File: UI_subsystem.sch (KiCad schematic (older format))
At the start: 1 part

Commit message: Created footprint and assigned it
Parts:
- TFT1: footprint (none) -> pwr_Beaglebone:ST7735
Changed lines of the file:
@@
 F 0 "TFT1" H 4550 1850 50  0000 R CNN
 F 1 "ST7735_TFT" H 4700 1950 50  0000 R CNN
-F 2 "" V 4527 1935 50  0001 C CNN
+F 2 "pwr_Beaglebone:ST7735" V 4527 1935 50  0001 C CNN
 F 3 "" V 4527 1935 50  0001 C CNN
 	1    3800 2750

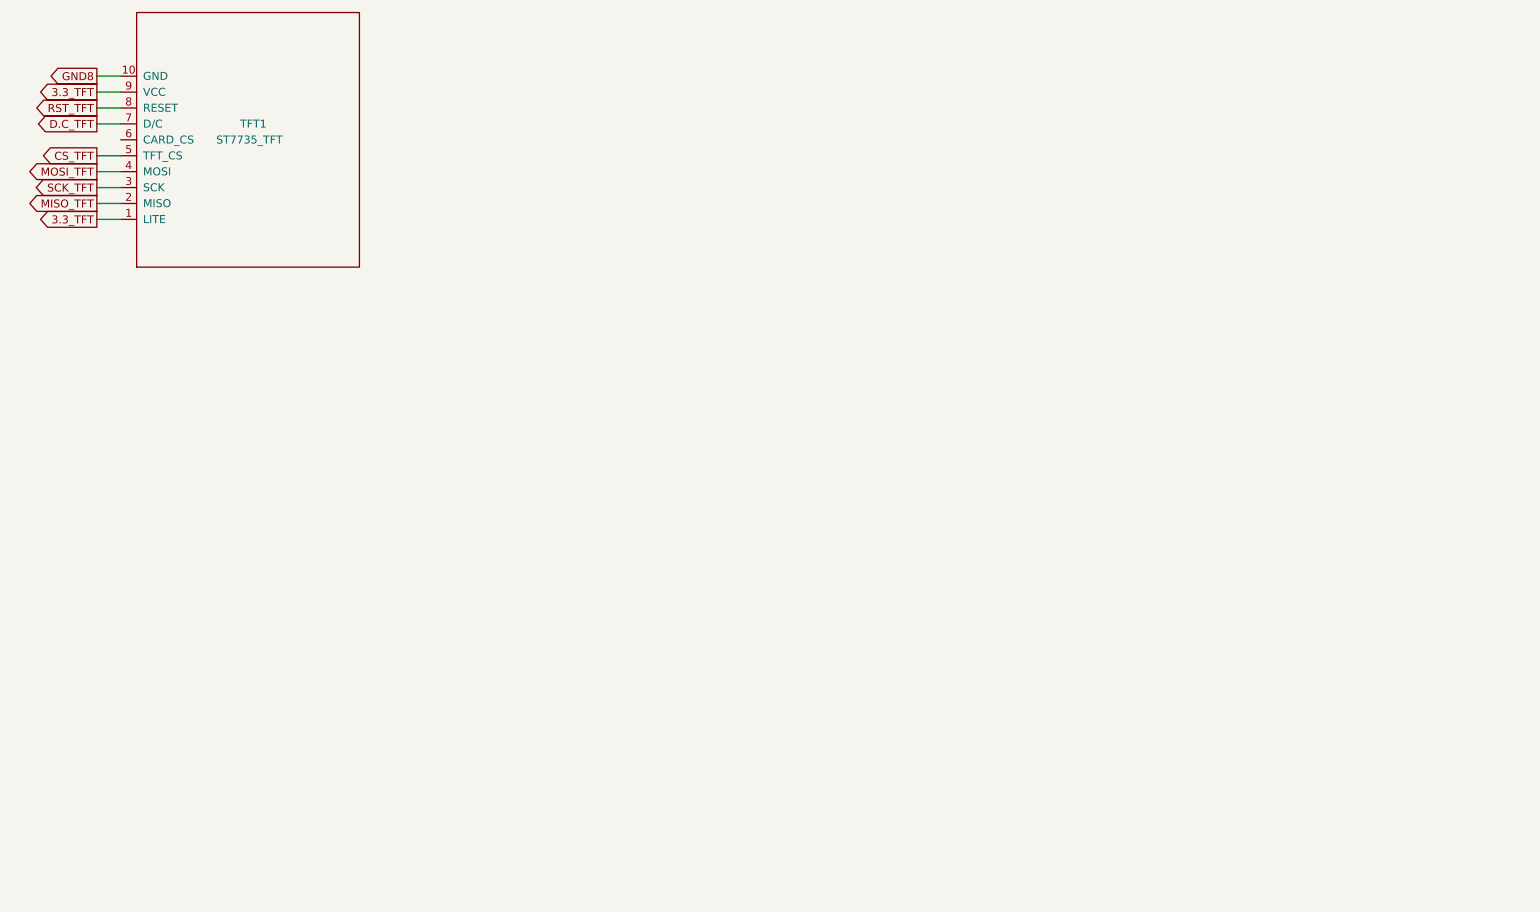
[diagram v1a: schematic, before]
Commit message: Added Buttons, LEDs and MCU to BB connections.
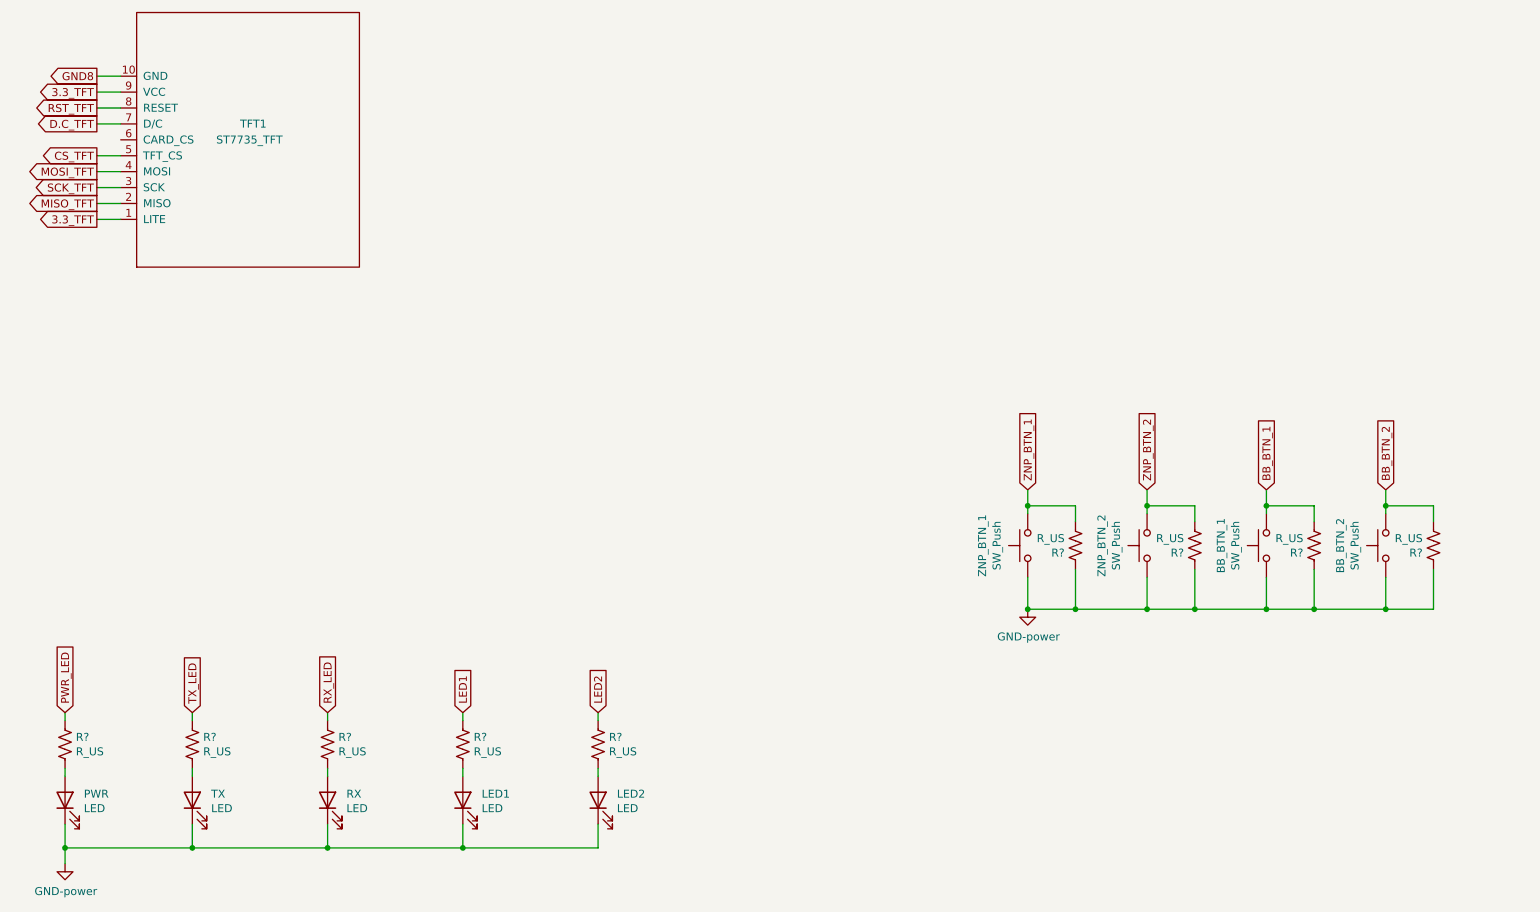
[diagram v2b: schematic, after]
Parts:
- added BB_BTN_1, BB_BTN_2, ZNP_BTN_1, ZNP_BTN_2: SW_Push, symbol Switch:SW_Push
- added LED1, LED2, PWR, RX, TX: LED, symbol Device:LED
- added R? (x9): R_US, symbol Device:R_US
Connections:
- new net: PWR.2 (A), R?.2
- new net: R?.2, TX.2 (A)
- new net: R?.2, RX.2 (A)
- new net: LED1.2 (A), R?.2
- new net: LED2.2 (A), R?.2
- new net BB_BTN_1: BB_BTN_1.2, R?.2
- new net BB_BTN_2: BB_BTN_2.2, R?.2
- new net GND: BB_BTN_1.1, BB_BTN_2.1, LED1.1 (K), LED2.1 (K), PWR.1 (K), R?.1, R?.1, R?.1, R?.1, RX.1 (K), TX.1 (K), ZNP_BTN_1.1, ZNP_BTN_2.1
- new net LED1: R?.1
- new net LED2: R?.1
- new net PWR_LED: R?.1
- new net RX_LED: R?.1
- new net TX_LED: R?.1
- new net ZNP_BTN_1: R?.2, ZNP_BTN_1.2
- new net ZNP_BTN_2: R?.2, ZNP_BTN_2.2

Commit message: Added Some Values
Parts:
- R? (x2): value R_US -> 100
- R? (x2): value R_US -> 10k
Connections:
- net labels added: +3V3
- wire segments 60 -> 50
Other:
- moved on the sheet: R?
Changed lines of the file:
@@
 $Descr A4 11693 8268
 encoding utf-8
-Sheet 1 5
+Sheet 1 1
 Title ""
 Date ""
@@
 L Device:R_US R?
 U 1 1 61481C85
-P 8300 4500
-F 0 "R?" H 8368 4546 50  0000 L CNN
-F 1 "R_US" H 8368 4455 50  0000 L CNN
-F 2 "" V 8340 4490 50  0001 C CNN
-F 3 "~" H 8300 4500 50  0001 C CNN
-	1    8300 4500
+P 8000 4000
+F 0 "R?" H 8068 4046 50  0000 L CNN
+F 1 "100" H 8068 3955 50  0000 L CNN
+F 2 "" V 8040 3990 50  0001 C CNN
+F 3 "~" H 8000 4000 50  0001 C CNN
+	1    8000 4000
 	-1   0    0    1
 $EndComp
-$Comp
-L Device:R_US R?
-U 1 1 61482BE5
-P 9050 4500
-F 0 "R?" H 9118 4546 50  0000 L CNN
-F 1 "R_US" H 9118 4455 50  0000 L CNN
-F 2 "" V 9090 4490 50  0001 C CNN
-F 3 "~" H 9050 4500 50  0001 C CNN
-	1    9050 4500
-	-1   0    0    1
-$EndComp
-$Comp
-L Device:R_US R?
-U 1 1 614833DA
-P 9800 4500
-F 0 "R?" H 9868 4546 50  0000 L CNN
-F 1 "R_US" H 9868 4455 50  0000 L CNN
-F 2 "" V 9840 4490 50  0001 C CNN
-F 3 "~" H 9800 4500 50  0001 C CNN
-	1    9800 4500
-	-1   0    0    1
-$EndComp
-$Comp
-L Device:R_US R?
-U 1 1 614839E0
-P 10550 4500
-F 0 "R?" H 10618 4546 50  0000 L CNN
-F 1 "R_US" H 10618 4455 50  0000 L CNN
-F 2 "" V 10590 4490 50  0001 C CNN
-F 3 "~" H 10550 4500 50  0001 C CNN
-	1    10550 4500
-	-1   0    0    1
-$EndComp
-Text GLabel 8000 4150 1    50   Input ~ 0
+Text GLabel 8000 3850 1    50   Input ~ 0
 ZNP_BTN_1
-Wire Wire Line
-	10550 4650 10550 4900
 Wire Wire Line
 	8000 4700 8000 4900
 Connection ~ 8000 4900
 Wire Wire Line
-	8300 4650 8300 4900
-Connection ~ 8300 4900
-Wire Wire Line
-	8300 4900 8000 4900
-Wire Wire Line
 	8750 4700 8750 4900
 Connection ~ 8750 4900
 Wire Wire Line
-	8750 4900 8300 4900
-Wire Wire Line
-	9050 4650 9050 4900
-Connection ~ 9050 4900
-Wire Wire Line
-	9050 4900 8750 4900
-Wire Wire Line
 	9500 4700 9500 4900
 Connection ~ 9500 4900
 Wire Wire Line
-	9500 4900 9050 4900
-Wire Wire Line
-	9800 4650 9800 4900
-Wire Wire Line
-	9500 4900 9800 4900
-Connection ~ 9800 4900
-Wire Wire Line
-	9800 4900 10250 4900
-Wire Wire Line
 	10250 4700 10250 4900
-Connection ~ 10250 4900
-Wire Wire Line
-	10250 4900 10550 4900
-Wire Wire Line
-	8300 4350 8300 4250
-Wire Wire Line
-	8300 4250 8000 4250
-Wire Wire Line
-	8000 4250 8000 4300
-Wire Wire Line
-	8000 4150 8000 4250
-Connection ~ 8000 4250
-Text GLabel 8750 4150 1    50   Input ~ 0
+Text GLabel 8750 3850 1    50   Input ~ 0
 ZNP_BTN_2
 Text GLabel 9500 4150 1    50   Input ~ 0
@@
 BB_BTN_2
 Wire Wire Line
-	8750 4150 8750 4250
-Wire Wire Line
 	9500 4150 9500 4250
 Wire Wire Line
 	10250 4150 10250 4250
-Wire Wire Line
-	9800 4350 9800 4250
 Wire Wire Line
 	9800 4250 9500 4250
@@
 	9500 4250 9500 4300
 Wire Wire Line
-	9050 4350 9050 4250
-Wire Wire Line
-	9050 4250 8750 4250
-Connection ~ 8750 4250
-Wire Wire Line
-	8750 4250 8750 4300
-Wire Wire Line
-	10550 4350 10550 4250
-Wire Wire Line
 	10550 4250 10250 4250
 Connection ~ 10250 4250
 Wire Wire Line
 	10250 4250 10250 4300
+Wire Wire Line
+	8000 4150 8000 4300
+Wire Wire Line
+	8750 4900 9500 4900
+Wire Wire Line
+	8750 4150 8750 4300
+Wire Wire Line
+	8000 4900 8750 4900
+Wire Wire Line
+	9500 4900 10250 4900
+Wire Wire Line
+	9800 4250 9800 4100
+Wire Wire Line
+	10550 4250 10550 4100
+$Comp
+L power:+3V3 #PWR?
+U 1 1 6149F0CA
+P 10550 3600
+F 0 "#PWR?" H 10550 3450 50  0001 C CNN
+F 1 "+3V3" H 10565 3773 50  0000 C CNN
+F 2 "" H 10550 3600 50  0001 C CNN
+F 3 "" H 10550 3600 50  0001 C CNN
+	1    10550 3600
+	1    0    0    -1
+$EndComp
+Wire Wire Line
+	9800 3800 9800 3650
+Wire Wire Line
+	9800 3650 10550 3650
+Wire Wire Line
+	10550 3650 10550 3600
+Wire Wire Line
+	10550 3800 10550 3650
+Connection ~ 10550 3650
+$Comp
+L Device:R_US R?
+U 1 1 61482BE5
+P 8750 4000
+F 0 "R?" H 8818 4046 50  0000 L CNN
+F 1 "100" H 8818 3955 50  0000 L CNN
+F 2 "" V 8790 3990 50  0001 C CNN
+F 3 "~" H 8750 4000 50  0001 C CNN
+	1    8750 4000
+	-1   0    0    1
+$EndComp
+$Comp
+L Device:R_US R?
+U 1 1 614833DA
+P 9800 3950
+F 0 "R?" H 9868 3996 50  0000 L CNN
+F 1 "10k" H 9868 3905 50  0000 L CNN
+F 2 "" V 9840 3940 50  0001 C CNN
+F 3 "~" H 9800 3950 50  0001 C CNN
+	1    9800 3950
+	-1   0    0    1
+$EndComp
+$Comp
+L Device:R_US R?
+U 1 1 614839E0
+P 10550 3950
+F 0 "R?" H 10618 3996 50  0000 L CNN
+F 1 "10k" H 10618 3905 50  0000 L CNN
+F 2 "" V 10590 3940 50  0001 C CNN
+F 3 "~" H 10550 3950 50  0001 C CNN
+	1    10550 3950
+	-1   0    0    1
+$EndComp
 $EndSCHEMATC

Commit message: Added JTAG to sch.
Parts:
- R? (x5): value R_US -> R
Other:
- moved on the sheet: BB_BTN_1, BB_BTN_2, R?, ZNP_BTN_1, ZNP_BTN_2
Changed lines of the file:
@@
 L Switch:SW_Push ZNP_BTN_1
 U 1 1 614536C0
-P 8000 4500
-F 0 "ZNP_BTN_1" H 8000 4785 50  0000 C CNN
-F 1 "SW_Push" H 8000 4694 50  0000 C CNN
-F 2 "" H 8000 4700 50  0001 C CNN
-F 3 "~" H 8000 4700 50  0001 C CNN
-	1    8000 4500
+P 6700 3800
+F 0 "ZNP_BTN_1" H 6700 4085 50  0000 C CNN
+F 1 "SW_Push" H 6700 3994 50  0000 C CNN
+F 2 "" H 6700 4000 50  0001 C CNN
+F 3 "~" H 6700 4000 50  0001 C CNN
+	1    6700 3800
 	0    -1   -1   0
 $EndComp
@@
 L Switch:SW_Push ZNP_BTN_2
 U 1 1 614542E2
-P 8750 4500
-F 0 "ZNP_BTN_2" H 8750 4785 50  0000 C CNN
-F 1 "SW_Push" H 8750 4694 50  0000 C CNN
-F 2 "" H 8750 4700 50  0001 C CNN
-F 3 "~" H 8750 4700 50  0001 C CNN
-	1    8750 4500
+P 7450 3800
+F 0 "ZNP_BTN_2" H 7450 4085 50  0000 C CNN
+F 1 "SW_Push" H 7450 3994 50  0000 C CNN
+F 2 "" H 7450 4000 50  0001 C CNN
+F 3 "~" H 7450 4000 50  0001 C CNN
+	1    7450 3800
 	0    -1   -1   0
 $EndComp
@@
 L Switch:SW_Push BB_BTN_1
 U 1 1 614544C6
-P 9500 4500
-F 0 "BB_BTN_1" H 9500 4785 50  0000 C CNN
-F 1 "SW_Push" H 9500 4694 50  0000 C CNN
-F 2 "" H 9500 4700 50  0001 C CNN
-F 3 "~" H 9500 4700 50  0001 C CNN
-	1    9500 4500
+P 8200 3800
+F 0 "BB_BTN_1" H 8200 4085 50  0000 C CNN
+F 1 "SW_Push" H 8200 3994 50  0000 C CNN
+F 2 "" H 8200 4000 50  0001 C CNN
+F 3 "~" H 8200 4000 50  0001 C CNN
+	1    8200 3800
 	0    -1   -1   0
 $EndComp
@@
 L Switch:SW_Push BB_BTN_2
 U 1 1 61454891
-P 10250 4500
-F 0 "BB_BTN_2" H 10250 4785 50  0000 C CNN
-F 1 "SW_Push" H 10250 4694 50  0000 C CNN
-F 2 "" H 10250 4700 50  0001 C CNN
-F 3 "~" H 10250 4700 50  0001 C CNN
-	1    10250 4500
+P 8950 3800
+F 0 "BB_BTN_2" H 8950 4085 50  0000 C CNN
+F 1 "SW_Push" H 8950 3994 50  0000 C CNN
+F 2 "" H 8950 4000 50  0001 C CNN
+F 3 "~" H 8950 4000 50  0001 C CNN
+	1    8950 3800
 	0    -1   -1   0
 $EndComp
@@
 P 1950 5750
 F 0 "R?" H 2018 5796 50  0000 L CNN
-F 1 "R_US" H 2018 5705 50  0000 L CNN
+F 1 "R" H 2018 5705 50  0000 L CNN
 F 2 "" V 1990 5740 50  0001 C CNN
 F 3 "~" H 1950 5750 50  0001 C CNN
@@
 P 2750 5750
 F 0 "R?" H 2818 5796 50  0000 L CNN
-F 1 "R_US" H 2818 5705 50  0000 L CNN
+F 1 "R" H 2818 5705 50  0000 L CNN
 F 2 "" V 2790 5740 50  0001 C CNN
 F 3 "~" H 2750 5750 50  0001 C CNN
@@
 P 3600 5750
 F 0 "R?" H 3668 5796 50  0000 L CNN
-F 1 "R_US" H 3668 5705 50  0000 L CNN
+F 1 "R" H 3668 5705 50  0000 L CNN
 F 2 "" V 3640 5740 50  0001 C CNN
 F 3 "~" H 3600 5750 50  0001 C CNN
@@
 P 4450 5750
 F 0 "R?" H 4518 5796 50  0000 L CNN
-F 1 "R_US" H 4518 5705 50  0000 L CNN
+F 1 "R" H 4518 5705 50  0000 L CNN
 F 2 "" V 4490 5740 50  0001 C CNN
 F 3 "~" H 4450 5750 50  0001 C CNN
@@
 P 5300 5750
 F 0 "R?" H 5368 5796 50  0000 L CNN
-F 1 "R_US" H 5368 5705 50  0000 L CNN
+F 1 "R" H 5368 5705 50  0000 L CNN
 F 2 "" V 5340 5740 50  0001 C CNN
 F 3 "~" H 5300 5750 50  0001 C CNN
@@
 L BeagleBone-Black-Cape-rescue:GND-power #PWR?
 U 1 1 61474E36
-P 8000 4900
-F 0 "#PWR?" H 8000 4650 50  0001 C CNN
-F 1 "GND-power" H 8005 4727 50  0000 C CNN
-F 2 "" H 8000 4900 50  0001 C CNN
-F 3 "" H 8000 4900 50  0001 C CNN
-	1    8000 4900
+P 6700 4200
+F 0 "#PWR?" H 6700 3950 50  0001 C CNN
+F 1 "GND-power" H 6705 4027 50  0000 C CNN
+F 2 "" H 6700 4200 50  0001 C CNN
+F 3 "" H 6700 4200 50  0001 C CNN
+	1    6700 4200
 	1    0    0    -1
 $EndComp
@@
 L Device:R_US R?
 U 1 1 61481C85
-P 8000 4000
-F 0 "R?" H 8068 4046 50  0000 L CNN
-F 1 "100" H 8068 3955 50  0000 L CNN
-F 2 "" V 8040 3990 50  0001 C CNN
-F 3 "~" H 8000 4000 50  0001 C CNN
-	1    8000 4000
+P 6700 3300
+F 0 "R?" H 6768 3346 50  0000 L CNN
+F 1 "100" H 6768 3255 50  0000 L CNN
+F 2 "" V 6740 3290 50  0001 C CNN
+F 3 "~" H 6700 3300 50  0001 C CNN
+	1    6700 3300
 	-1   0    0    1
 $EndComp
-Text GLabel 8000 3850 1    50   Input ~ 0
+Text GLabel 6700 3150 1    50   Input ~ 0
 ZNP_BTN_1
 Wire Wire Line
-	8000 4700 8000 4900
-Connection ~ 8000 4900
-Wire Wire Line
-	8750 4700 8750 4900
-Connection ~ 8750 4900
-Wire Wire Line
-	9500 4700 9500 4900
-Connection ~ 9500 4900
-Wire Wire Line
-	10250 4700 10250 4900
-Text GLabel 8750 3850 1    50   Input ~ 0
+	6700 4000 6700 4200
+Connection ~ 6700 4200
+Wire Wire Line
+	7450 4000 7450 4200
+Connection ~ 7450 4200
+Wire Wire Line
+	8200 4000 8200 4200
+Connection ~ 8200 4200
+Wire Wire Line
+	8950 4000 8950 4200
+Text GLabel 7450 3150 1    50   Input ~ 0
 ZNP_BTN_2
-Text GLabel 9500 4150 1    50   Input ~ 0
+Text GLabel 8200 3450 1    50   Input ~ 0
 BB_BTN_1
-Text GLabel 10250 4150 1    50   Input ~ 0
+Text GLabel 8950 3450 1    50   Input ~ 0
 BB_BTN_2
 Wire Wire Line
-	9500 4150 9500 4250
-Wire Wire Line
-	10250 4150 10250 4250
-Wire Wire Line
-	9800 4250 9500 4250
-Connection ~ 9500 4250
-Wire Wire Line
-	9500 4250 9500 4300
-Wire Wire Line
-	10550 4250 10250 4250
-Connection ~ 10250 4250
-Wire Wire Line
-	10250 4250 10250 4300
-Wire Wire Line
-	8000 4150 8000 4300
-Wire Wire Line
-	8750 4900 9500 4900
-Wire Wire Line
-	8750 4150 8750 4300
-Wire Wire Line
-	8000 4900 8750 4900
-Wire Wire Line
-	9500 4900 10250 4900
-Wire Wire Line
-	9800 4250 9800 4100
-Wire Wire Line
-	10550 4250 10550 4100
+	8200 3450 8200 3550
+Wire Wire Line
+	8950 3450 8950 3550
+Wire Wire Line
+	8500 3550 8200 3550
+Connection ~ 8200 3550
+Wire Wire Line
+	8200 3550 8200 3600
+Wire Wire Line
+	9250 3550 8950 3550
+Connection ~ 8950 3550
+Wire Wire Line
+	8950 3550 8950 3600
+Wire Wire Line
+	6700 3450 6700 3600
+Wire Wire Line
+	7450 4200 8200 4200
+Wire Wire Line
+	7450 3450 7450 3600
+Wire Wire Line
+	6700 4200 7450 4200
+Wire Wire Line
+	8200 4200 8950 4200
+Wire Wire Line
+	8500 3550 8500 3400
+Wire Wire Line
+	9250 3550 9250 3400
 $Comp
 L power:+3V3 #PWR?
 U 1 1 6149F0CA
-P 10550 3600
-F 0 "#PWR?" H 10550 3450 50  0001 C CNN
-F 1 "+3V3" H 10565 3773 50  0000 C CNN
-F 2 "" H 10550 3600 50  0001 C CNN
-F 3 "" H 10550 3600 50  0001 C CNN
-	1    10550 3600
-	1    0    0    -1
-$EndComp
-Wire Wire Line
-	9800 3800 9800 3650
-Wire Wire Line
-	9800 3650 10550 3650
-Wire Wire Line
-	10550 3650 10550 3600
-Wire Wire Line
-	10550 3800 10550 3650
-Connection ~ 10550 3650
+P 9250 2900
+F 0 "#PWR?" H 9250 2750 50  0001 C CNN
+F 1 "+3V3" H 9265 3073 50  0000 C CNN
+F 2 "" H 9250 2900 50  0001 C CNN
+F 3 "" H 9250 2900 50  0001 C CNN
+	1    9250 2900
+	1    0    0    -1
+$EndComp
+Wire Wire Line
+	8500 3100 8500 2950
+Wire Wire Line
+	8500 2950 9250 2950
+Wire Wire Line
+	9250 2950 9250 2900
+Wire Wire Line
+	9250 3100 9250 2950
+Connection ~ 9250 2950
 $Comp
 L Device:R_US R?
 U 1 1 61482BE5
-P 8750 4000
-F 0 "R?" H 8818 4046 50  0000 L CNN
-F 1 "100" H 8818 3955 50  0000 L CNN
-F 2 "" V 8790 3990 50  0001 C CNN
-F 3 "~" H 8750 4000 50  0001 C CNN
-	1    8750 4000
+P 7450 3300
+F 0 "R?" H 7518 3346 50  0000 L CNN
+F 1 "100" H 7518 3255 50  0000 L CNN
+F 2 "" V 7490 3290 50  0001 C CNN
+F 3 "~" H 7450 3300 50  0001 C CNN
+	1    7450 3300
 	-1   0    0    1
 $EndComp
@@
 L Device:R_US R?
 U 1 1 614833DA
-P 9800 3950
-F 0 "R?" H 9868 3996 50  0000 L CNN
-F 1 "10k" H 9868 3905 50  0000 L CNN
-F 2 "" V 9840 3940 50  0001 C CNN
-F 3 "~" H 9800 3950 50  0001 C CNN
-	1    9800 3950
+P 8500 3250
+F 0 "R?" H 8568 3296 50  0000 L CNN
+F 1 "10k" H 8568 3205 50  0000 L CNN
+F 2 "" V 8540 3240 50  0001 C CNN
+F 3 "~" H 8500 3250 50  0001 C CNN
+	1    8500 3250
 	-1   0    0    1
 $EndComp
@@
 L Device:R_US R?
 U 1 1 614839E0
-P 10550 3950
-F 0 "R?" H 10618 3996 50  0000 L CNN
-F 1 "10k" H 10618 3905 50  0000 L CNN
-F 2 "" V 10590 3940 50  0001 C CNN
-F 3 "~" H 10550 3950 50  0001 C CNN
-	1    10550 3950
+P 9250 3250
+F 0 "R?" H 9318 3296 50  0000 L CNN
+F 1 "10k" H 9318 3205 50  0000 L CNN
+F 2 "" V 9290 3240 50  0001 C CNN
+F 3 "~" H 9250 3250 50  0001 C CNN
+	1    9250 3250
 	-1   0    0    1
 $EndComp
